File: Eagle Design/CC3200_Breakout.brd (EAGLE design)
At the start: 58.4 x 35.2 mm, 47 parts, among them J22 M10X2, J23 M10X2, U15 AT25FS010, Y2 32.768KHz, Y3 407MHz

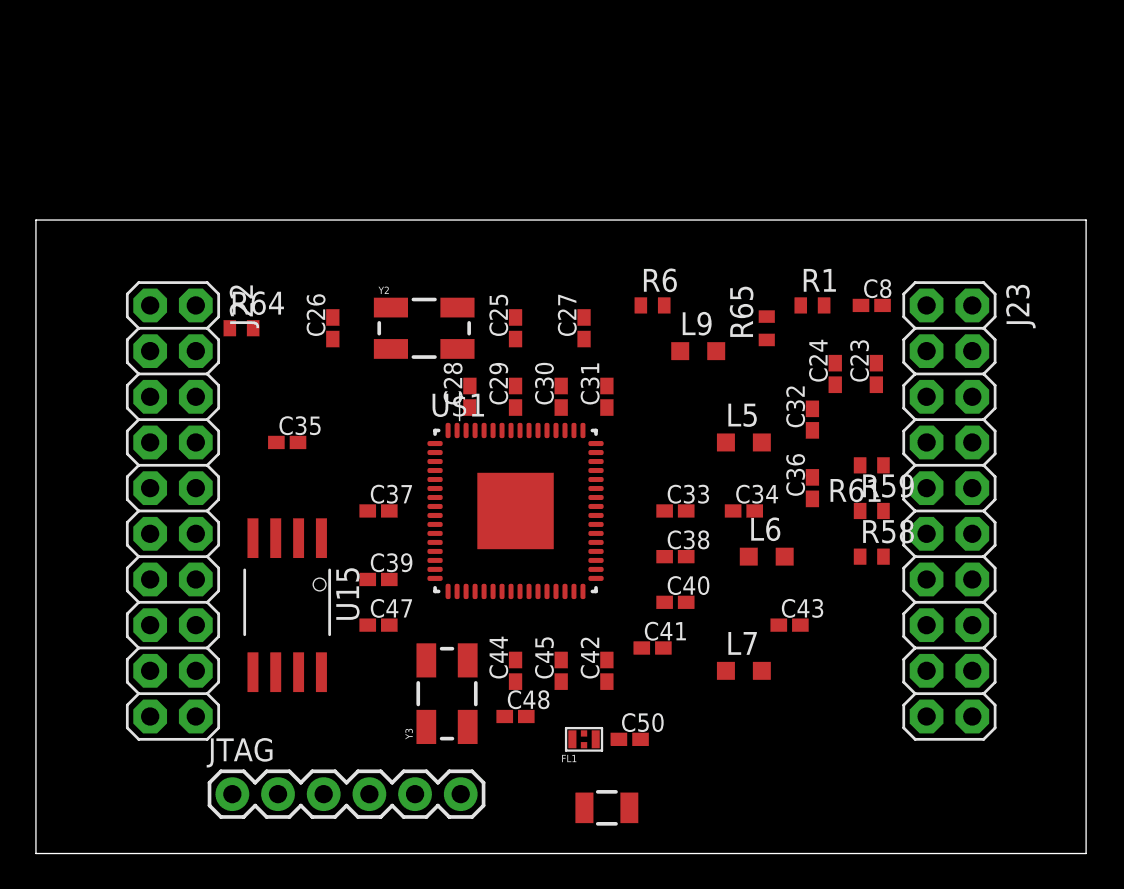
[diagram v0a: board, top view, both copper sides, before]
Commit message: SOP
Added SOP connector and addition connector JP90 to be use as jumper wire
used in Energia
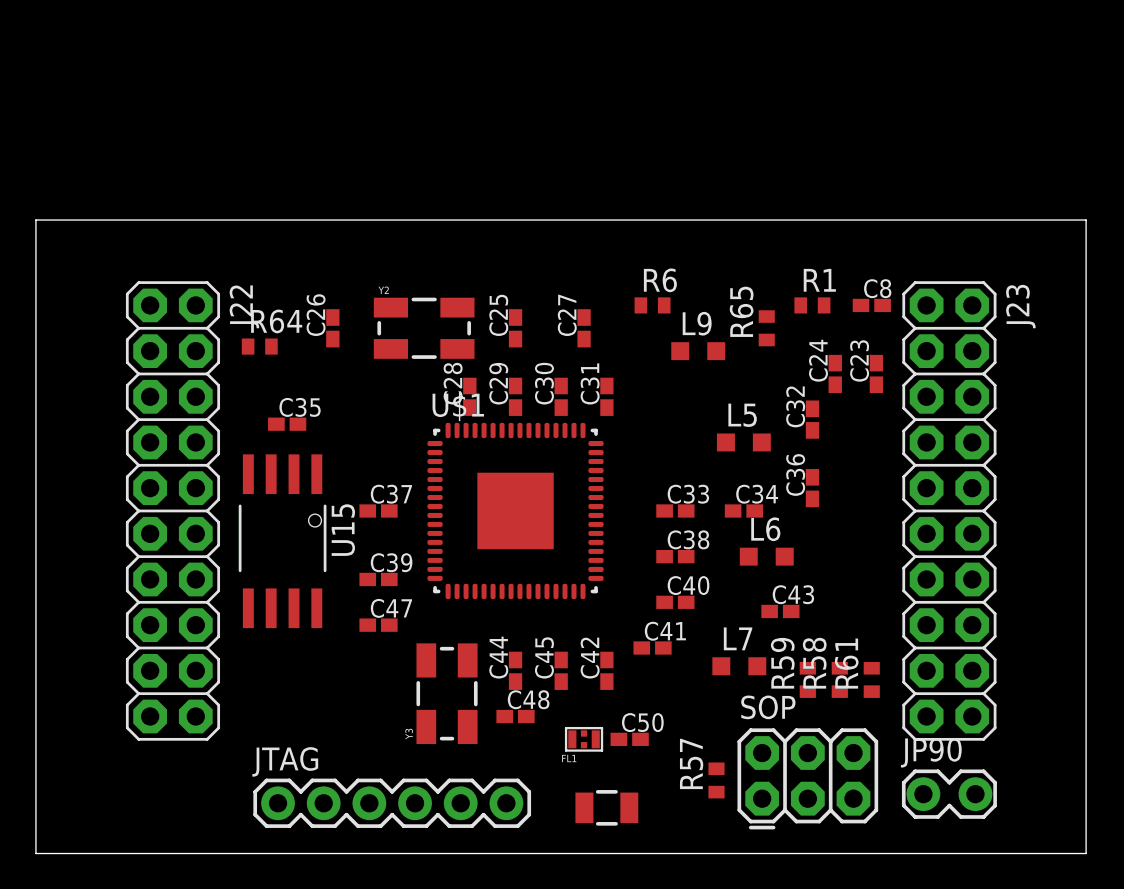
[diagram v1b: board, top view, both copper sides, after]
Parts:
- added JP90: M02LOCK, SparkFun-Connectors:1X02_LOCK
- added R57: 1k, resistor:R0402
- added SOP: (no value), SparkFun-Connectors:2X3
- R58, R59: value 100k -> 1k
- R61: value 2.7k -> 1k
- moved R61 11.9 mm to (46.5, 9.65), turned to 90 degrees
- moved R59 10.0 mm to (42.9, 9.65), turned to 90 degrees
- moved R58 7.08 mm to (44.7, 9.65), turned to 90 degrees
- moved U15 3.57 mm to (13.7, 17.5)
- moved JTAG 2.59 mm to (13.5, 2.79)
- moved R64 1.44 mm to (12.4, 28.2)
- moved C35 1.02 mm to (14.0, 23.9)
- moved C43 0.92 mm to (41.4, 13.5)
- moved L7 0.36 mm to (39.1, 10.4)
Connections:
- new net N$6: R57.2, SOP.2, SOP.4, SOP.6
- net GND: now also R58.1, R59.1, R61.1; no longer R58.2, R59.2, R61.2
- net JTAG_TCK: now also JP90.1
- net N$13: now also R59.2, SOP.5; no longer R59.1
- net N$21: now also R58.2, SOP.3; no longer R58.1
- net N$22: now also JP90.2, R61.2, SOP.1; no longer R61.1
- net VCC_BRD: now also R57.1

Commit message: Routing
Add connector for Battery JP91
Start Routing
Added design rule for and Gerber of smart-prototyping.
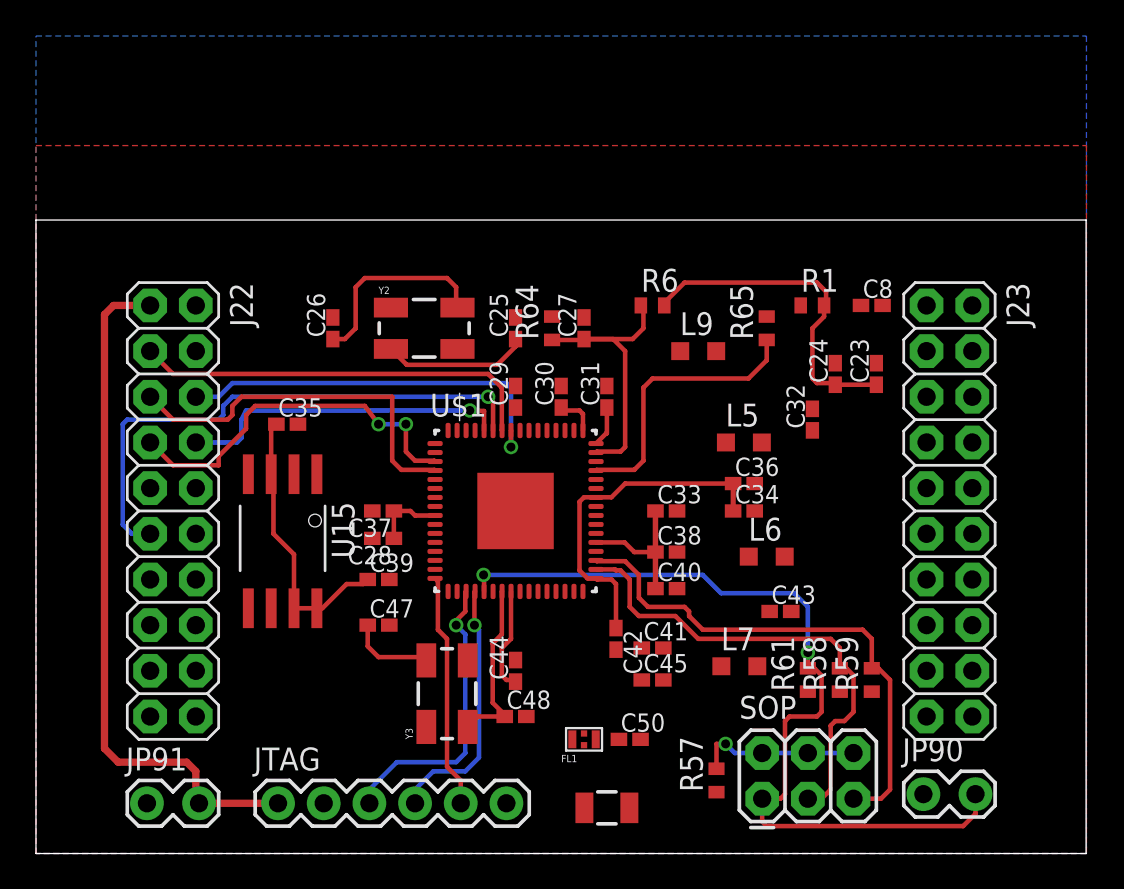
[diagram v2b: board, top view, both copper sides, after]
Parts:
- added JP91: M02LOCK, SparkFun-Connectors:1X02_LOCK
- moved R64 16.3 mm to (28.7, 29.2), turned to 90 degrees
- moved C28 9.24 mm to (19.3, 17.5), turned to 180 degrees
- moved C45 5.11 mm to (34.3, 9.65), turned to 0 degrees
- moved C36 3.82 mm to (39.4, 20.6), turned to 0 degrees
- moved R59 3.56 mm to (46.5, 9.65)
- moved R61 3.56 mm to (42.9, 9.65)
- moved C42 1.85 mm to (32.3, 11.9), turned to 270 degrees
- moved C40 0.92 mm to (35.1, 14.7)
- moved C38 0.57 mm to (35.1, 16.8)
- moved C33 0.51 mm to (35.1, 19.1)
- moved C37 0.25 mm to (19.3, 19.1), turned to 180 degrees
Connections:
- net GND: now also JP91.1
- net VCC_BRD: now also JP91.2
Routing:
- net N$22: track 0.00 -> 48.4 mm, vias 0 -> 2
- net V_BATT: track 0.00 -> 42.2 mm
- net VCC_BRD: track 0.00 -> 38.7 mm
- net 59: track 0.00 -> 30.6 mm, vias 0 -> 1
- net N$13: track 0.00 -> 29.3 mm
- net N$21: track 0.00 -> 27.0 mm
- net 58: track 0.00 -> 22.8 mm
- net 57: track 0.00 -> 22.2 mm, vias 0 -> 1
- net 4: track 0.00 -> 21.0 mm
- net 3: track 0.00 -> 20.7 mm, vias 0 -> 2
- net N$10: track 0.00 -> 20.5 mm
- net 60: track 0.00 -> 18.6 mm, vias 0 -> 1
- net JTAG_TCK: track 0.00 -> 16.4 mm, vias 0 -> 1
- net N$20: track 0.00 -> 16.3 mm
- net N$12: track 0.00 -> 15.5 mm
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- added copper zone on layer 1, net GND
- added copper zone on layer 16, net GND

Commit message: 4 Layers and routing
Made PCB 4 Layers and more routing, plus vias under mcu
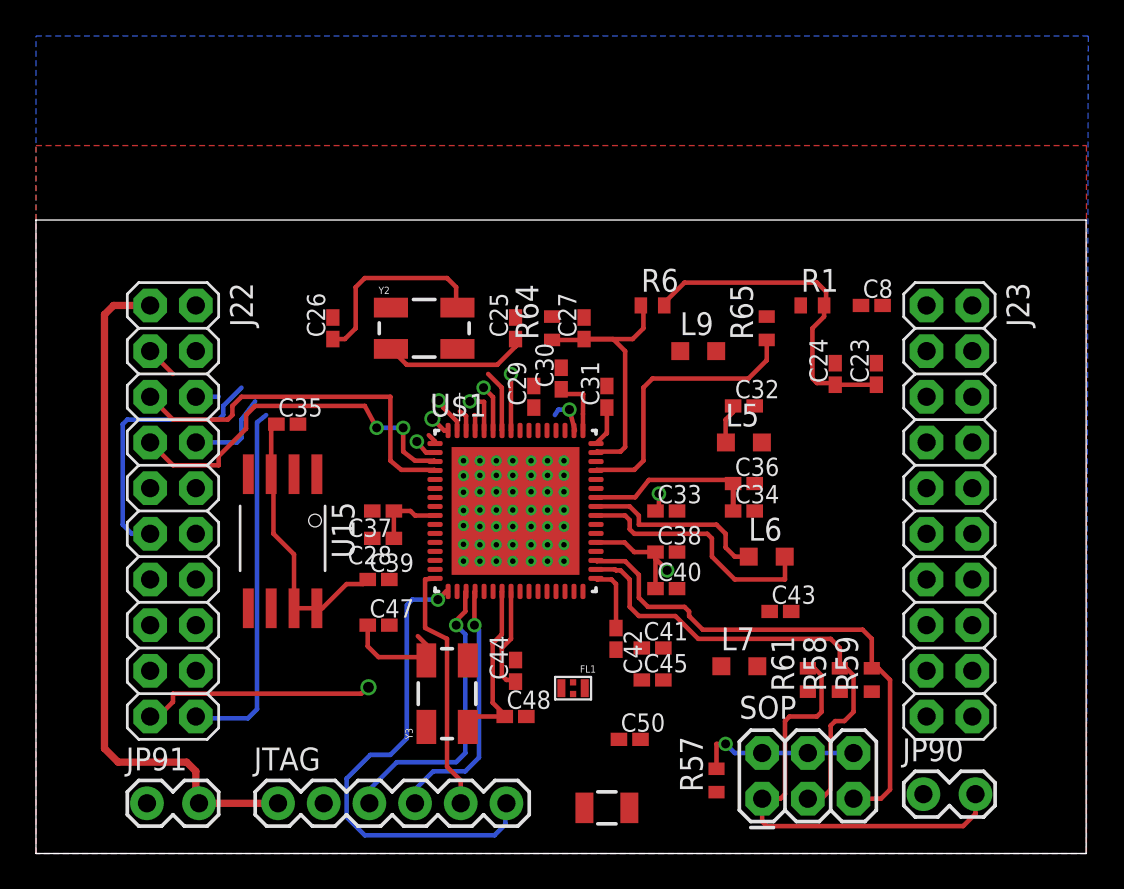
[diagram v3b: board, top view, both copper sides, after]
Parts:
- moved C32 3.89 mm to (39.4, 24.9), turned to 0 degrees
- moved FL1 2.91 mm to (29.9, 9.19), turned to 180 degrees
- moved C30 1.02 mm to (29.2, 26.4)
- moved C29 1.02 mm to (27.7, 25.4)
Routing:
- net SDA: track 0.00 -> 30.7 mm, vias 0 -> 2
- net 64: track 0.00 -> 28.0 mm, vias 0 -> 1
- net JTAG_TDO: track 0.00 -> 27.1 mm, vias 0 -> 1
- net 63: track 0.00 -> 24.7 mm, vias 0 -> 1
- net N$22: track 48.4 -> 25.3 mm, vias 2 -> 0
- net 50: track 0.00 -> 22.5 mm, vias 0 -> 1
- net 58: track 22.8 -> 5.26 mm
- net 57: track 22.2 -> 4.68 mm
- net N$7: track 0.00 -> 14.2 mm
- net 59: track 30.6 -> 17.7 mm
- net 60: track 18.6 -> 7.31 mm
- net N$8: track 0.00 -> 10.4 mm
- net N$10: track 20.5 -> 14.9 mm
- net V_BATT: track 42.2 -> 46.7 mm, vias 0 -> 2
- net N$17: track 3.92 -> 6.13 mm
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- added copper zone on layer 2, net GND
- added copper zone on layer 15, net VCC_BRD
- added copper zone on layer 16, net VCC_BRD
- removed copper zone on layer 16, net GND

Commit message: Routing
Almost finished routing except Anttena
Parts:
- moved L9 24.2 mm to (27.0, 5.84)
- moved C45 11.7 mm to (44.5, 15.4)
- moved C41 11.5 mm to (44.5, 16.9)
- moved L7 9.92 mm to (44.8, 18.5)
- moved C37 8.51 mm to (16.2, 11.1)
- moved C28 8.41 mm to (16.2, 9.70)
- moved C8 6.50 mm to (40.0, 30.6), turned to 180 degrees
- moved C50 4.70 mm to (28.8, 4.27)
- moved C29 4.32 mm to (27.5, 29.7)
- moved C43 3.06 mm to (44.5, 13.7)
- moved R64 2.35 mm to (30.7, 30.5)
- moved C30 2.24 mm to (31.3, 27.2), turned to 0 degrees
- moved C27 1.95 mm to (32.0, 30.4)
- moved U$3 1.27 mm to (30.5, 2.59)
- moved C25 1.18 mm to (25.6, 29.7)
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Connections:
- removed net N$34: R65.2
- net 45: now also R65.2
- net VCC_BRD: no longer JP91.2, JTAG.1, R57.1
- net V_BATT: now also JP91.2, JTAG.1, R57.1
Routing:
- net JTAG_TCK: track 16.4 -> 145.4 mm
- net 18: track 0.00 -> 118.9 mm, vias 0 -> 3
- net 15: track 0.00 -> 56.0 mm, vias 0 -> 1
- net 55: track 0.00 -> 52.9 mm, vias 0 -> 1
- net SPI_MISO: track 0.00 -> 50.4 mm, vias 0 -> 1
- net N$17: track 6.13 -> 54.0 mm, vias 0 -> 4
- net V_BATT: track 46.7 -> 94.5 mm, vias 2 -> 8
- net SPI_MOSI: track 0.00 -> 47.6 mm, vias 0 -> 2
- net SPI_CS: track 0.00 -> 45.9 mm, vias 0 -> 1
- net 53: track 0.00 -> 45.4 mm, vias 0 -> 3
- net VCC_BRD: track 38.7 -> 0.00 mm
- net 50: track 22.5 -> 60.7 mm
- net SCL: track 0.61 -> 30.5 mm, vias 0 -> 1
- net N$14: track 0.00 -> 29.8 mm, vias 0 -> 2
- net N$3: track 2.27 -> 31.5 mm, vias 0 -> 2
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- added copper zone on layer 15, net V_BATT
- removed copper zone on layer 15, net VCC_BRD

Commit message: Antenna
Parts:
- removed L9: 3.6nH, resistor:L2012C
- added L1: (no value), Spark:C0402
- moved C50 3.11 mm to (30.5, 6.86)
- moved U$3 3.03 mm to (33.3, 1.42)
- moved FL1 2.90 mm to (29.9, 12.1)
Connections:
- net N$36: now also L1.1; no longer L9.1
- net N$37: now also L1.2; no longer L9.2
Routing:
- net N$37: track 0.00 -> 9.27 mm
- net N$9: track 0.00 -> 2.16 mm
- net 45: track 20.8 -> 22.8 mm
- net N$36: track 0.00 -> 1.87 mm
- added copper zone on layer 1, net N$15
- added copper zone on layer 1, net N$16
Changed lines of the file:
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@@
 <layer number="56" name="wert" color="7" fill="1" visible="no" active="no"/>
 <layer number="57" name="tCAD" color="7" fill="1" visible="no" active="no"/>
+<layer number="59" name="tCarbon" color="7" fill="1" visible="yes" active="yes"/>
+<layer number="60" name="bCarbon" color="7" fill="1" visible="yes" active="yes"/>
 <layer number="90" name="Modules" color="5" fill="1" visible="no" active="no"/>
 <layer number="91" name="Nets" color="2" fill="1" visible="no" active="no"/>
@@
 <layer number="127" name="_tValues" color="7" fill="1" visible="yes" active="yes"/>
 <layer number="128" name="_bValues" color="7" fill="1" visible="yes" active="yes"/>
+<layer number="129" name="Mask" color="7" fill="1" visible="yes" active="yes"/>
 <layer number="131" name="tAdjust" color="7" fill="1" visible="yes" active="yes"/>
 <layer number="132" name="bAdjust" color="7" fill="1" visible="yes" active="yes"/>
@@
 </autorouter>
 <elements>
-<element name="FL1" library="DEA202450" package="DEA202450" value="DEA202450" x="29.8704" y="9.1948" rot="R180"/>
+<element name="FL1" library="DEA202450" package="DEA202450" value="DEA202450" x="29.9212" y="12.0904" rot="R180"/>
 <element name="C40" library="resistor" package="C0402K" value="4.7uF" x="35.56" y="14.8844"/>
 <element name="C41" library="resistor" package="C0402K" value="0.1uF" x="44.45" y="16.8656"/>
@@
 <element name="C24" library="resistor" package="C0402K" value="100uF" x="44.45" y="26.67" rot="R90"/>
 <element name="C8" library="resistor" package="C0402K" value="0.8uF" x="39.9796" y="30.6324" rot="R180"/>
-<element name="C50" library="resistor" package="C0402K" value="1.0pF" x="28.8036" y="4.2672"/>
+<element name="C50" library="resistor" package="C0402K" value="1.0pF" x="30.5308" y="6.858"/>
 <element name="L7" library="resistor" package="L2012C" value="2.2uH" x="44.8056" y="18.542"/>
 <element name="L6" library="resistor" package="L2012C" value="1uH" x="40.64" y="16.51"/>
 <element name="L5" library="resistor" package="L2012C" value="2.2uH" x="39.37" y="22.86"/>
-<element name="L9" library="resistor" package="L2012C" value="3.6nH" x="26.9748" y="5.842"/>
 <element name="R1" library="resistor" package="R0402" value="100k" x="43.18" y="30.48"/>
 <element name="R64" library="resistor" package="R0402" value="" x="30.6832" y="30.48" rot="R90"/>
@@
 <element name="U$1" library="cc3200" package="PVQFN-N64" value="CC3200" x="26.67" y="19.05"/>
 <element name="U15" library="SparkFun-DigitalIC" package="SO08WIDE" value="AT25FS010" x="13.716" y="17.526" rot="R180"/>
-<element name="U$3" library="SparkFun-RF" package="ANTENNA-CHIP2" value="ANTENNA2SMD" x="30.48" y="2.5908" rot="R90"/>
+<element name="U$3" library="SparkFun-RF" package="ANTENNA-CHIP2" value="ANTENNA2SMD" x="33.274" y="1.4224" rot="R90"/>
 <element name="J22" library="SparkFun-Connectors" package="2X10" value="M10X2" x="7.62" y="19.05" locked="yes" rot="R270"/>
 <element name="J23" library="SparkFun-Connectors" package="2X10" value="M10X2" x="50.8" y="19.05" locked="yes" rot="R270"/>
@@
 <element name="R61" library="resistor" package="R0402" value="1k" x="42.926" y="9.652" rot="R90"/>
 <element name="JP91" library="SparkFun-Connectors" package="1X02_LOCK" value="M02LOCK" x="6.35" y="2.794"/>
+<element name="L1" library="Spark" package="C0402" value="" x="29.9212" y="9.2456" rot="R270"/>
 </elements>
 <signals>
@@
 <contactref element="U$1" pad="31"/>
 <contactref element="FL1" pad="1"/>
-<wire x1="29.8704" y1="9.5198" x2="29.92" y2="14.575" width="0" layer="19" extent="1-1"/>
+<wire x1="29.92" y1="14.575" x2="29.9212" y2="14.575" width="0" layer="19" extent="1-16"/>
+<wire x1="29.9212" y1="12.4154" x2="29.9212" y2="14.0208" width="0.4572" layer="1"/>
+<wire x1="29.92" y1="14.575" x2="29.9212" y2="14.575" width="0.3048" layer="1"/>
+<wire x1="29.9212" y1="14.575" x2="29.9212" y2="14.0208" width="0.3048" layer="1"/>
 </signal>
 <signal name="N$36">
 <contactref element="FL1" pad="3"/>
-<contactref element="L9" pad="1"/>
-<wire x1="29.8704" y1="8.8698" x2="25.9748" y2="5.842" width="0" layer="19" extent="1-1"/>
+<contactref element="L1" pad="1"/>
+<wire x1="29.9212" y1="11.7654" x2="29.9212" y2="9.8956" width="0.4572" layer="1"/>
 </signal>
 <signal name="N$37">
-<contactref element="L9" pad="2"/>
 <contactref element="C50" pad="1"/>
 <contactref element="U$3" pad="FEED"/>
-<wire x1="28.2036" y1="4.2672" x2="27.9748" y2="5.842" width="0" layer="19" extent="1-1"/>
-<wire x1="29.23" y1="2.5908" x2="28.2036" y2="4.2672" width="0" layer="19" extent="1-1"/>
+<contactref element="L1" pad="2"/>
+<wire x1="29.9212" y1="8.5956" x2="29.9308" y2="8.5956" width="0.4572" layer="1"/>
+<wire x1="29.9308" y1="8.5956" x2="29.9308" y2="6.858" width="0.4572" layer="1"/>
+<wire x1="29.9308" y1="6.858" x2="29.9412" y2="1.4224" width="0.4572" layer="1"/>
+<wire x1="29.9412" y1="1.4224" x2="32.024" y2="1.4224" width="0.4572" layer="1"/>
 </signal>
 <signal name="VCC_BRD">
@@
 <contactref element="J23" pad="8"/>
 <contactref element="R65" pad="2"/>
-<wire x1="52.07" y1="22.86" x2="42.2148" y2="22.86" width="0.254" layer="15"/>
-<wire x1="42.2148" y1="22.86" x2="42.0624" y2="23.0124" width="0.254" layer="15"/>
-<wire x1="42.0624" y1="23.0124" x2="42.0624" y2="27.686" width="0.254" layer="15"/>
+<wire x1="52.07" y1="22.86" x2="51.308" y2="21.6408" width="0.254" layer="15"/>
+<wire x1="51.308" y1="21.6408" x2="42.0624" y2="21.6408" width="0.254" layer="15"/>
+<wire x1="42.0624" y1="21.6408" x2="42.0624" y2="27.686" width="0.254" layer="15"/>
 <wire x1="42.0624" y1="27.686" x2="41.6052" y2="28.1432" width="0.254" layer="15"/>
 <wire x1="41.6052" y1="28.1432" x2="38.9636" y2="28.1432" width="0.254" layer="15"/>
@@
 <wire x1="37.846" y1="6.096" x2="37.846" y2="4.714" width="0.254" layer="1"/>
 </signal>
+<signal name="N$15">
+<polygon width="0.4572" layer="1" pour="cutout">
+<vertex x="28.6004" y="6.4516"/>
+<vertex x="35.3568" y="6.4516"/>
+<vertex x="35.3568" y="2.54"/>
+<vertex x="28.6004" y="2.54"/>
+</polygon>
+</signal>
+<signal name="N$16">
+<polygon width="0.4572" layer="1" pour="cutout">
+<vertex x="29.4132" y="14.1732"/>
+<vertex x="30.4292" y="14.1732"/>
+<vertex x="30.4292" y="6.5532"/>
+<vertex x="29.4132" y="6.5532"/>
+</polygon>
+</signal>
 </signals>
